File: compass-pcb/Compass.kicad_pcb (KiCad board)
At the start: 2 copper layers, 81.3 x 81.7 mm, 24 parts

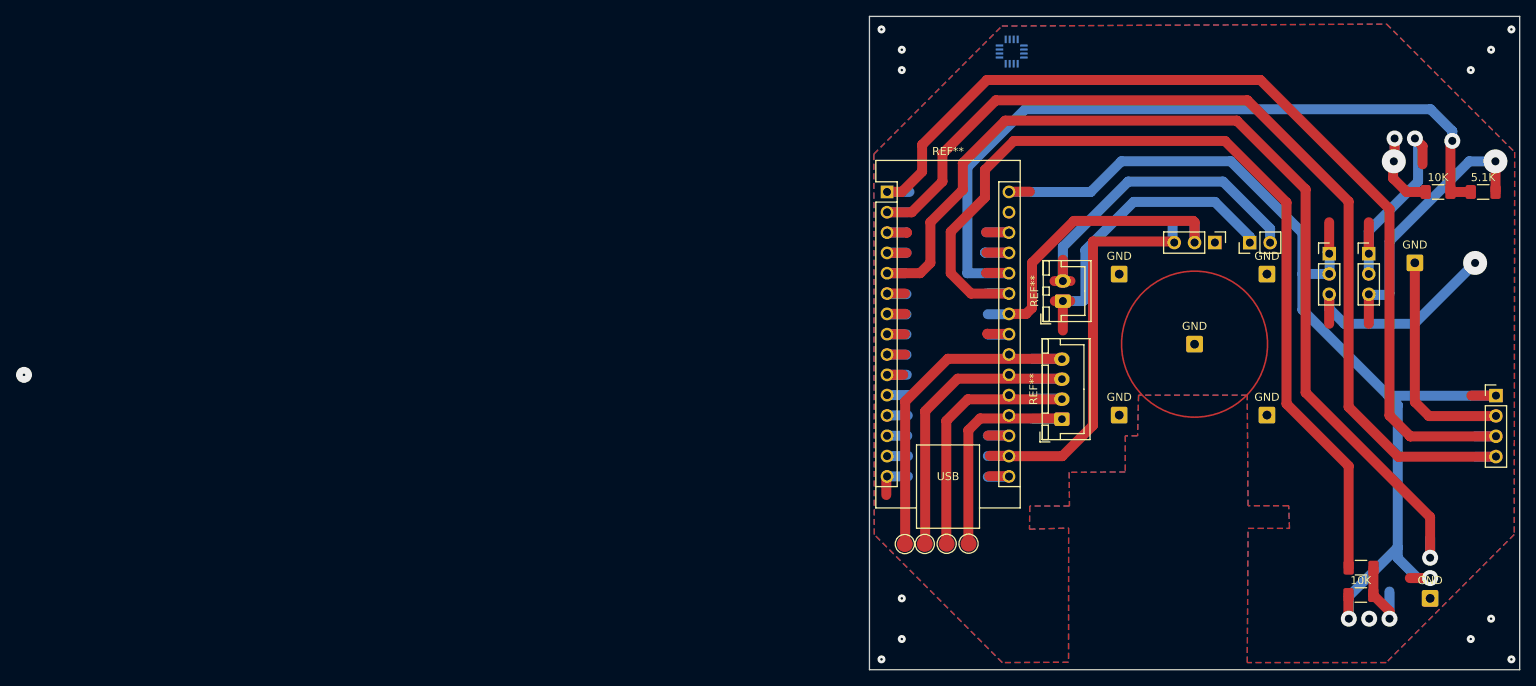
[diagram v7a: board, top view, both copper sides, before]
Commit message: pcb border (shape)
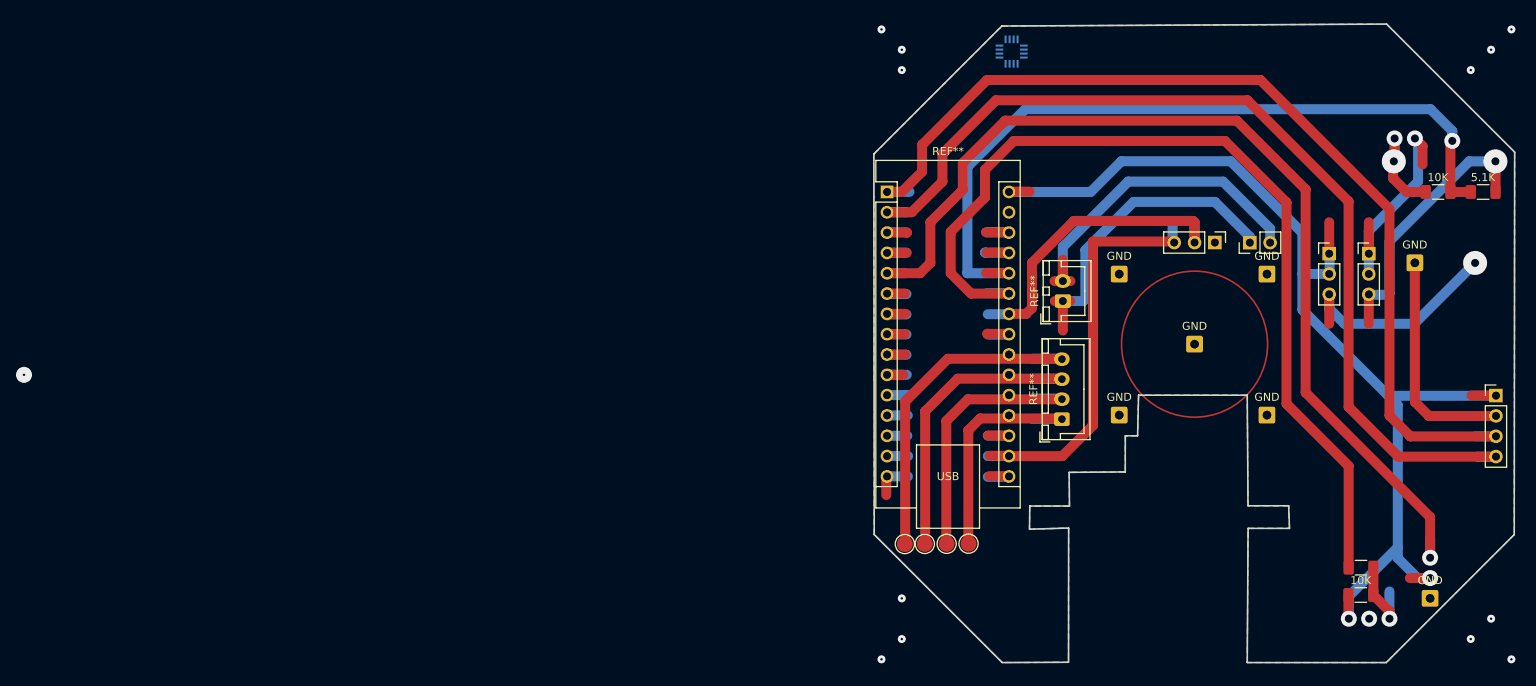
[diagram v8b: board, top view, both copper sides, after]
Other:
- board size 81.3 x 81.7 mm -> 80.1 x 79.8 mm
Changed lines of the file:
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@@
   (gr_circle (center 147.32 93.98) (end 156.445445 93.98)
     (stroke (width 0.2) (type default)) (fill none) (layer "F.Cu"))
-  (gr_rect (start 106.68 53.010655) (end 187.96 134.675526)
-    (stroke (width 0.1) (type default)) (fill none) (layer "Edge.Cuts"))
+  (gr_poly
+    (pts
+      (xy 153.905445 133.781331)
+      (xy 154.010859 117.007204)
+      (xy 159.18796 117.007204)
+      (xy 159.082546 114.180214)
+      (xy 154.002546 114.180214)
+      (xy 153.905445 100.358533)
+      (xy 140.320868 100.358533)
+      (xy 140.198825 105.438533)
+      (xy 138.665445 105.438533)
+      (xy 138.657483 109.949925)
+      (xy 131.644012 110.005694)
+      (xy 131.684396 114.212124)
+      (xy 126.721204 114.214815)
+      (xy 126.685996 117.111261)
+      (xy 131.579599 116.965392)
+      (xy 131.566462 133.744901)
+      (xy 123.281198 133.781331)
+      (xy 107.281198 117.781331)
+      (xy 107.233111 70.214117)
+      (xy 123.233111 54.214117)
+      (xy 171.330346 53.97315)
+      (xy 187.330346 69.97315)
+      (xy 187.282258 117.781331)
+      (xy 171.282258 133.781331)
+    )
+    (stroke (width 0.2) (type solid)) (fill none) (layer "Edge.Cuts"))
   (gr_text "Servo\n(A)" (at 181.845445 123.218533 90) (layer "B.SilkS")
     (effects (font (size 1 1.5) (thickness 0.25) bold) (justify bottom))
